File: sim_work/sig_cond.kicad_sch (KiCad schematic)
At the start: 13 parts, among them U1 LM741, U2 LM741

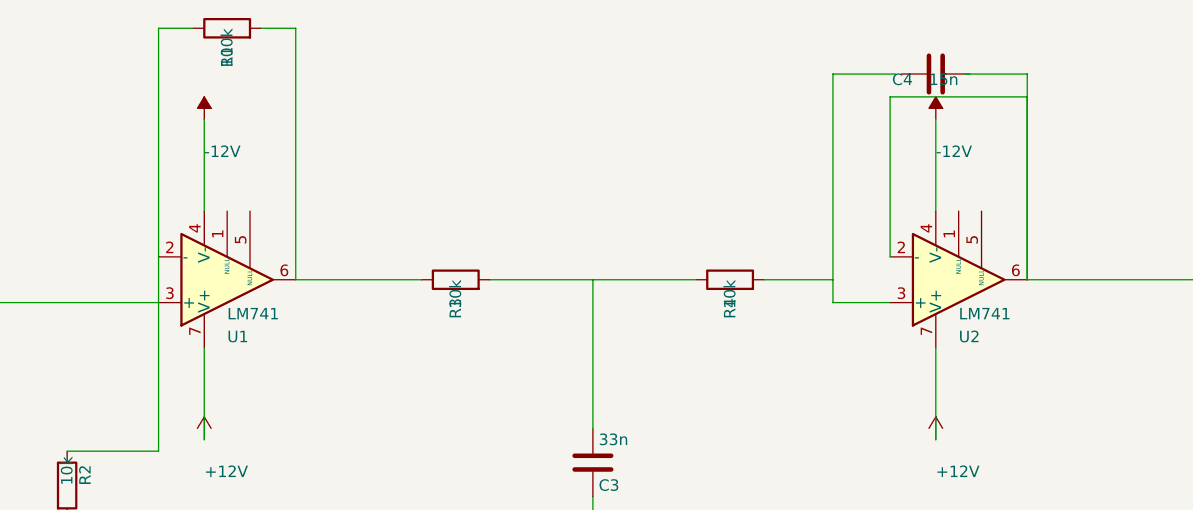
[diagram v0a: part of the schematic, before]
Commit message: Add comparison mode, fix SimGUI subprocess popups, DAC7800 IC boxes
- SimGUI: fix Python path detection (FindPython searches Python312/313/311)
- SimGUI: suppress console popup windows (CREATE_NO_WINDOW for subprocess)
- SimGUI: add Comparison project (MDAC vs Analog oscillator side-by-side)
- SimGUI: fix async wrapping (direct await instead of Task.Run)
- Pipeline: draw DAC7800 as proper IC box with pin labels (VREF/IOUT/VCTRL)
- Pipeline: fix electrometer_362 layout (spacing, junction dots at T-junctions)
- Pipeline: fix summing amp gain annotations (BP=-0.455, not -2.2)
- Pipeline: add analog_osc command for friend's SVF oscillator simulation
- Docs: comparison_guide.md, updated README and PROJECT tracker

Co-Authored-By: Claude Opus 4.6 <noreply@anthropic.com>
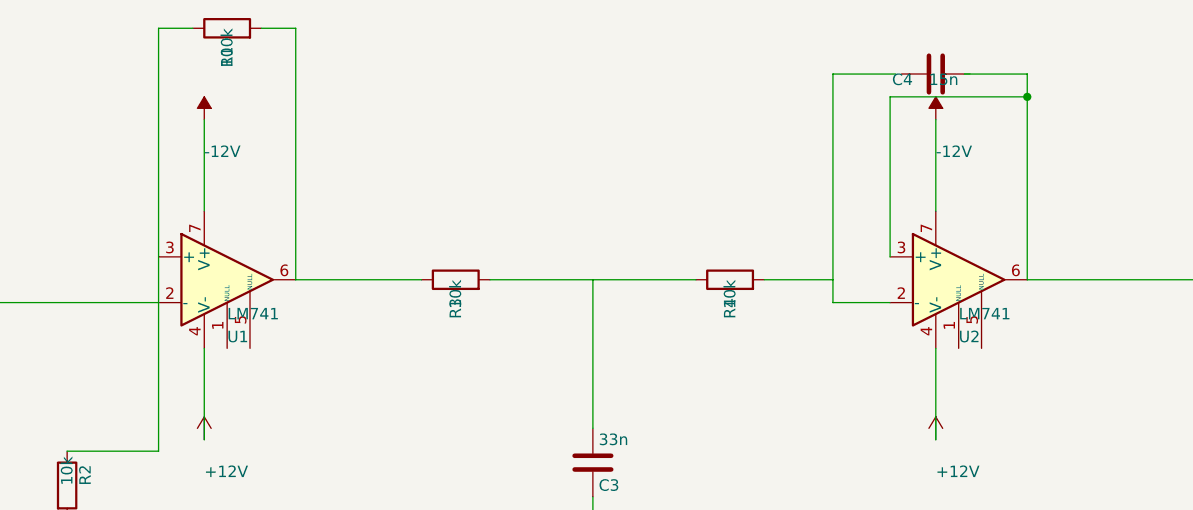
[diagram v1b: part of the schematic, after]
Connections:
- net +12V: now also U1.4 (V-), U2.4 (V-); no longer U1.7 (V+), U2.7 (V+)
- net -12V: now also U1.7 (V+), U2.7 (V+); no longer U1.4 (V-), U2.4 (V-)
- net at R1.1, R2.1: now also U1.3 (+); no longer U1.2 (-)
- net at C2.1, U2.6: now also U2.3 (+); no longer U2.2 (-)
- net at R4.2: now also U2.2 (-); no longer U2.3 (+)
- net at C1.2: now also U1.2 (-); no longer U1.3 (+)
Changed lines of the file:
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@@
 		(lib_id "LM741:LM741")
 		(at 106.68 96.52 0)
-		(mirror x)
 		(unit 1)
 		(exclude_from_sim no)
@@
 		(instances
 			(project "Signal Conditioner"
-				(path "/ca6782c8-9cda-40c0-914e-ddd08bfb183d"
+				(path "/d5dc8867-4f50-4e93-aa1c-31461e1099ae"
 					(reference "U1")
 					(unit 1)
@@
 		(lib_id "LM741:LM741")
 		(at 187.96 96.52 0)
-		(mirror x)
 		(unit 1)
 		(exclude_from_sim no)
@@
 		(instances
 			(project "Signal Conditioner"
-				(path "/ca6782c8-9cda-40c0-914e-ddd08bfb183d"
+				(path "/d5dc8867-4f50-4e93-aa1c-31461e1099ae"
 					(reference "U2")
 					(unit 1)
@@
 		(instances
 			(project "Signal Conditioner"
-				(path "/ca6782c8-9cda-40c0-914e-ddd08bfb183d"
+				(path "/d5dc8867-4f50-4e93-aa1c-31461e1099ae"
 					(reference "R1")
 					(unit 1)
@@
 		(instances
 			(project "Signal Conditioner"
-				(path "/ca6782c8-9cda-40c0-914e-ddd08bfb183d"
+				(path "/d5dc8867-4f50-4e93-aa1c-31461e1099ae"
 					(reference "R2")
 					(unit 1)
@@
 		(instances
 			(project "Signal Conditioner"
-				(path "/ca6782c8-9cda-40c0-914e-ddd08bfb183d"
+				(path "/d5dc8867-4f50-4e93-aa1c-31461e1099ae"
 					(reference "C1")
 					(unit 1)
@@
 		(instances
 			(project "Signal Conditioner"
-				(path "/ca6782c8-9cda-40c0-914e-ddd08bfb183d"
+				(path "/d5dc8867-4f50-4e93-aa1c-31461e1099ae"
 					(reference "R3")
 					(unit 1)
@@
 		(instances
 			(project "Signal Conditioner"
-				(path "/ca6782c8-9cda-40c0-914e-ddd08bfb183d"
+				(path "/d5dc8867-4f50-4e93-aa1c-31461e1099ae"
 					(reference "R4")
 					(unit 1)
@@
 		(instances
 			(project "Signal Conditioner"
-				(path "/ca6782c8-9cda-40c0-914e-ddd08bfb183d"
+				(path "/d5dc8867-4f50-4e93-aa1c-31461e1099ae"
 					(reference "C3")
 					(unit 1)
@@
 		(instances
 			(project "Signal Conditioner"
-				(path "/ca6782c8-9cda-40c0-914e-ddd08bfb183d"
+				(path "/d5dc8867-4f50-4e93-aa1c-31461e1099ae"
 					(reference "C4")
 					(unit 1)
@@
 		(instances
 			(project "Signal Conditioner"
-				(path "/ca6782c8-9cda-40c0-914e-ddd08bfb183d"
+				(path "/d5dc8867-4f50-4e93-aa1c-31461e1099ae"
 					(reference "C2")
 					(unit 1)
@@
 		(instances
 			(project "Signal Conditioner"
-				(path "/ca6782c8-9cda-40c0-914e-ddd08bfb183d"
+				(path "/d5dc8867-4f50-4e93-aa1c-31461e1099ae"
 					(reference "R6")
 					(unit 1)
@@
 		(instances
 			(project "Signal Conditioner"
-				(path "/ca6782c8-9cda-40c0-914e-ddd08bfb183d"
+				(path "/d5dc8867-4f50-4e93-aa1c-31461e1099ae"
 					(reference "R5")
 					(unit 1)
@@
 		(instances
 			(project "Signal Conditioner"
-				(path "/ca6782c8-9cda-40c0-914e-ddd08bfb183d"
+				(path "/d5dc8867-4f50-4e93-aa1c-31461e1099ae"
 					(reference "#PWR01")
 					(unit 1)
@@
 		(instances
 			(project "Signal Conditioner"
-				(path "/ca6782c8-9cda-40c0-914e-ddd08bfb183d"
+				(path "/d5dc8867-4f50-4e93-aa1c-31461e1099ae"
 					(reference "#PWR02")
 					(unit 1)
@@
 		(instances
 			(project "Signal Conditioner"
-				(path "/ca6782c8-9cda-40c0-914e-ddd08bfb183d"
+				(path "/d5dc8867-4f50-4e93-aa1c-31461e1099ae"
 					(reference "#PWR03")
 					(unit 1)
@@
 		(instances
 			(project "Signal Conditioner"
-				(path "/ca6782c8-9cda-40c0-914e-ddd08bfb183d"
+				(path "/d5dc8867-4f50-4e93-aa1c-31461e1099ae"
 					(reference "#PWR04")
 					(unit 1)
@@
 		(instances
 			(project "Signal Conditioner"
-				(path "/ca6782c8-9cda-40c0-914e-ddd08bfb183d"
+				(path "/d5dc8867-4f50-4e93-aa1c-31461e1099ae"
 					(reference "#PWR05")
 					(unit 1)
@@
 		(instances
 			(project "Signal Conditioner"
-				(path "/ca6782c8-9cda-40c0-914e-ddd08bfb183d"
+				(path "/d5dc8867-4f50-4e93-aa1c-31461e1099ae"
 					(reference "#PWR06")
 					(unit 1)
@@
 		(instances
 			(project "Signal Conditioner"
-				(path "/ca6782c8-9cda-40c0-914e-ddd08bfb183d"
+				(path "/d5dc8867-4f50-4e93-aa1c-31461e1099ae"
 					(reference "#PWR07")
 					(unit 1)
@@
 		(instances
 			(project "Signal Conditioner"
-				(path "/ca6782c8-9cda-40c0-914e-ddd08bfb183d"
+				(path "/d5dc8867-4f50-4e93-aa1c-31461e1099ae"
 					(reference "#PWR08")
 					(unit 1)
@@
 		(instances
 			(project "Signal Conditioner"
-				(path "/ca6782c8-9cda-40c0-914e-ddd08bfb183d"
+				(path "/d5dc8867-4f50-4e93-aa1c-31461e1099ae"
 					(reference "V1")
 					(unit 1)
@@
 		(instances
 			(project "Signal Conditioner"
-				(path "/ca6782c8-9cda-40c0-914e-ddd08bfb183d"
+				(path "/d5dc8867-4f50-4e93-aa1c-31461e1099ae"
 					(reference "#PWR09")
 					(unit 1)
@@
 	(wire
 		(pts
+			(xy 180.34 93.98) (xy 180.34 76.2)
+		)
+		(stroke
+			(width 0)
+			(type default)
+		)
+	)
+	(wire
+		(pts
+			(xy 180.34 76.2) (xy 195.58 76.2)
+		)
+		(stroke
+			(width 0)
+			(type default)
+		)
+	)
+	(wire
+		(pts
 			(xy 195.58 73.66) (xy 195.58 96.52)
 		)
@@
 	(wire
 		(pts
-			(xy 180.34 93.98) (xy 180.34 76.2)
-		)
-		(stroke
-			(width 0)
-			(type default)
-		)
-	)
-	(wire
-		(pts
-			(xy 180.34 76.2) (xy 195.58 76.2)
-		)
-		(stroke
-			(width 0)
-			(type default)
-		)
-	)
-	(wire
-		(pts
-			(xy 195.58 76.2) (xy 195.58 96.52)
-		)
-		(stroke
-			(width 0)
-			(type default)
-		)
-	)
-	(wire
-		(pts
 			(xy 195.58 96.52) (xy 222.25 96.52)
 		)
@@
 		)
 	)
+	(junction
+		(at 195.58 76.2)
+		(diameter 0)
+		(color 0 0 0 0)
+	)
 	(label "OUT"
